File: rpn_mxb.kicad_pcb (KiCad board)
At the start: 2 copper layers, 76.2 x 127 mm, 70 parts, among them J1 Conn_01x16_Female, J2 Conn_01x05_Female, J3 USB_B_Micro, Q1 Q_NMOS_GSD, Q2 Q_NMOS_GSD, SW1 SW_Push, SW10 SW_Push, SW11 SW_Push, SW12 SW_Push, SW13 SW_Push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

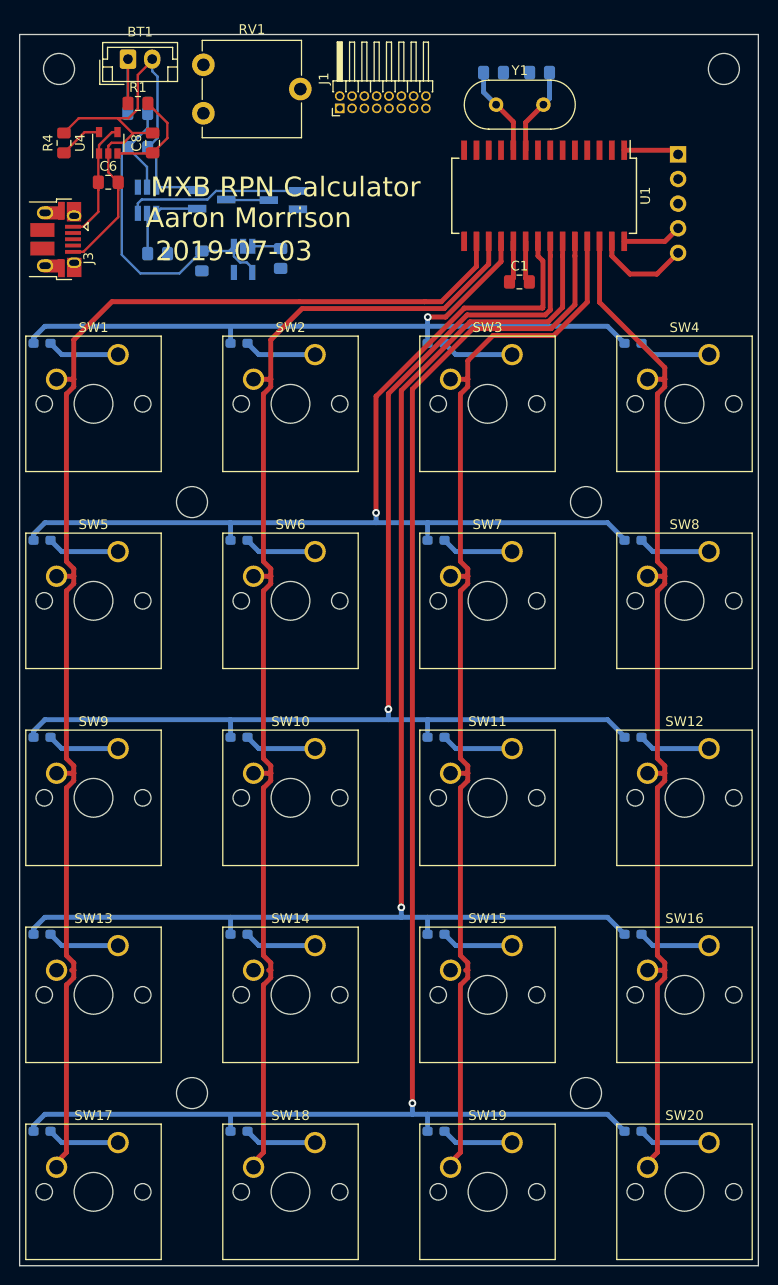
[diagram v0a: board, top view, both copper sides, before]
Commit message: DFM version
Add ability for microcontroller to enable/disable backlight, fix bug
with where BATT net comes from, create gerbers to submit to DFM.
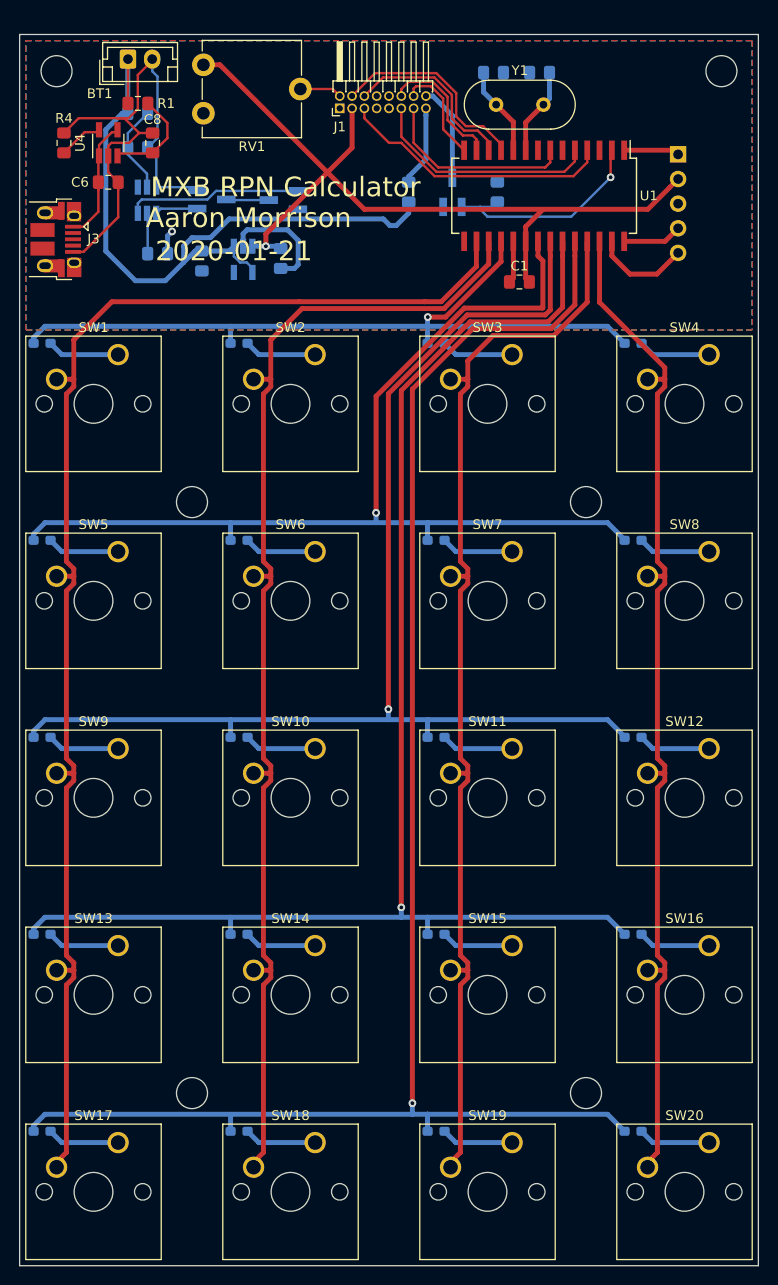
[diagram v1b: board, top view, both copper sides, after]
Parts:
- removed the REF** at (110.7, 36.6)
- removed the REF** at (179.3, 36.6)
- added Q3: Q_NMOS_GSD, Package_TO_SOT_SMD:SOT-23_Handsoldering, B.Cu at (151.3, 49.3)
- added R5: R_US, Resistor_SMD:R_0805_2012Metric_Pad1.15x1.40mm_HandSolder, B.Cu at (146.8, 49.3)
- added R6: R_US, Resistor_SMD:R_0805_2012Metric_Pad1.15x1.40mm_HandSolder, B.Cu at (156.0, 49.3)
- added REF**: MountingHole_3.2mm_M3, MountingHole:MountingHole_3.2mm_M3, F.Cu at (110.5, 36.8)
- added REF**: MountingHole_3.2mm_M3, MountingHole:MountingHole_3.2mm_M3, F.Cu at (179.1, 36.8)
- U4: footprint Package_TO_SOT_SMD:SOT-23-5 -> Package_TO_SOT_SMD:SOT-23-5_HandSoldering
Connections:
- BT1 pad 1: Net-(BT1-Pad1) -> +BATT
- C7 pad 1: +BATT -> Net-(C7-Pad1)
- R1 pad 1: Net-(BT1-Pad1) -> +BATT
- R2 pad 1: +BATT -> Net-(C7-Pad1)
- R2 pad 2: Net-(BT1-Pad1) -> +BATT
- U1 pad 11: /DB7 -> /RS
- U1 pad 12: /RW -> /E
- U1 pad 13: /E -> /DB5
- U1 pad 14: /DB4 -> /DB7
- U1 pad 2: Net-(U1-Pad2) -> /BL_EN
- U1 pad 4: /DB5 -> /RW
- U1 pad 5: /DB6 -> /DB4
- U1 pad 7: /RS -> /DB6
- U3 pad 5: +BATT -> Net-(C7-Pad1)
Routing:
- net +3V3: track 7.37 -> 85.8 mm, vias 0 -> 1
- net +BATT: track 38.0 -> 73.5 mm
- net /RW: track 0.00 -> 28.3 mm
- net /DB4: track 0.00 -> 23.9 mm
- net /BL_EN: track 0.00 -> 22.5 mm, vias 0 -> 1
- net /RS: track 0.00 -> 21.4 mm
- net /DB6: track 0.00 -> 20.2 mm
- net /E: track 0.00 -> 18.7 mm
- net GND: track 4.36 -> 18.9 mm, vias 0 -> 1
- net /DB5: track 0.00 -> 13.8 mm
- net /DB7: track 0.00 -> 10.7 mm
- net Net-(BT1-Pad1): track 10.2 -> 0.00 mm
- net /LED-: track 0.00 -> 9.97 mm
- net Net-(C7-Pad1): track 0.00 -> 9.29 mm
- net /LED+: track 0.00 -> 8.36 mm
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- added copper zone on B.Cu, net GND
- added copper zone on F.Cu, net GND
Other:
- rule trace_min: 0.2 -> 0.249936
- board text added: "2020-01-21"
- board text added: "~MCLR~ 3v3"
- board text removed: "2019-07-03"
